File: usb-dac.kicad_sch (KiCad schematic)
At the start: 18 parts, among them P1 USB_C_Plug_USB2.0, U1 PCM2912APJTR, Y1 6 Mhz

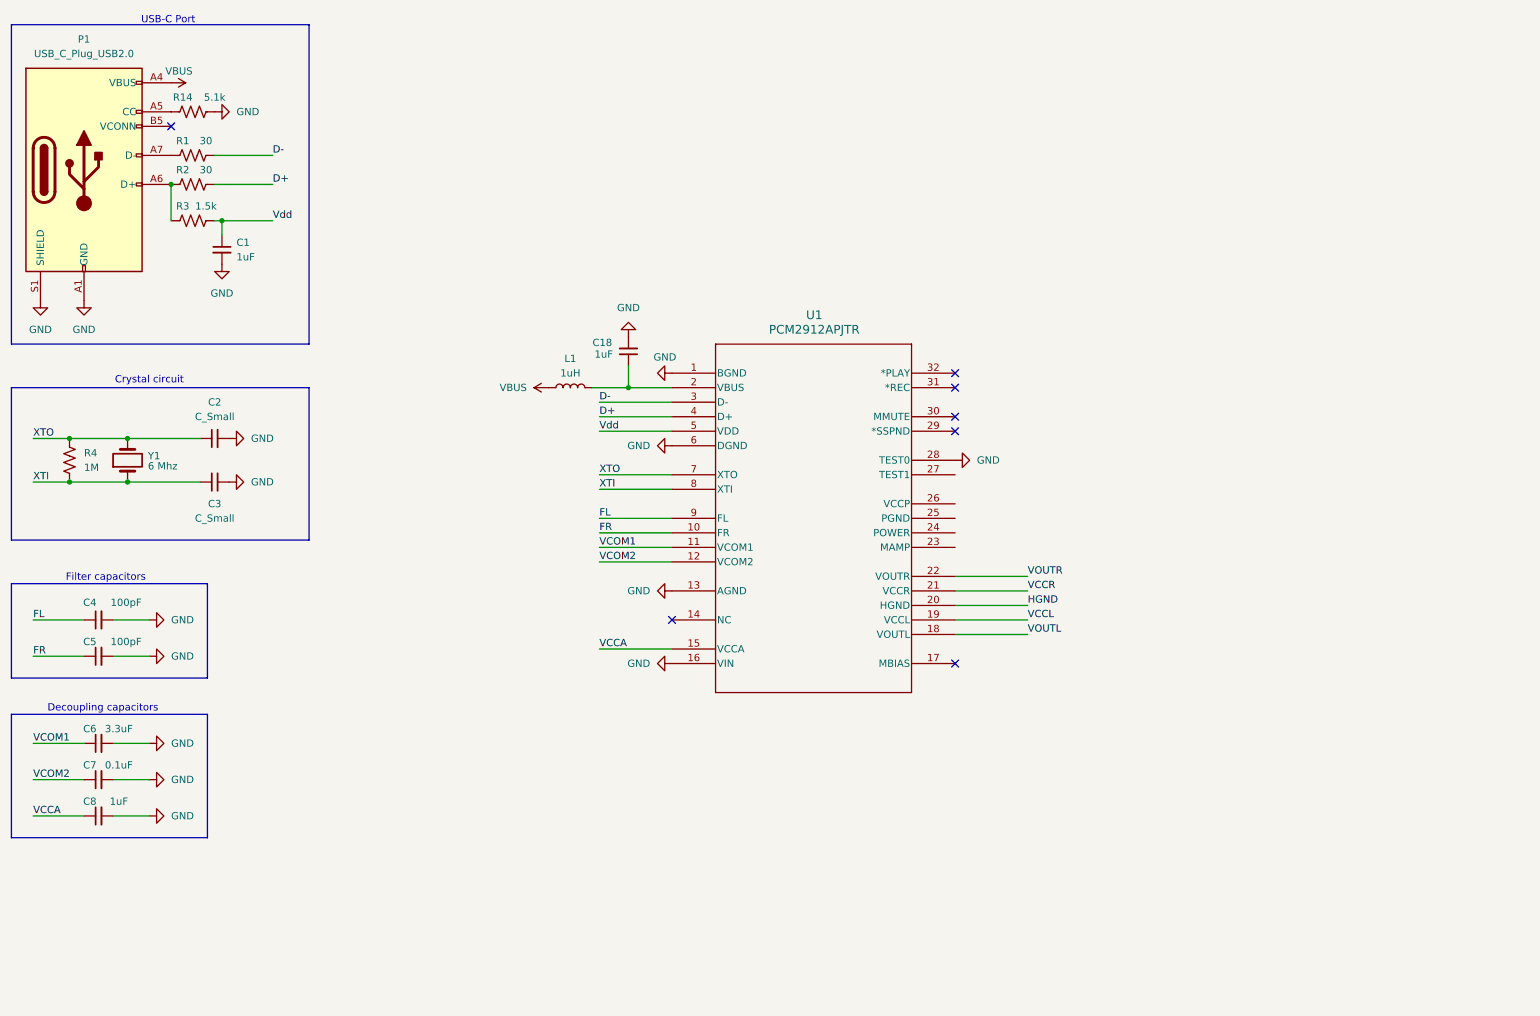
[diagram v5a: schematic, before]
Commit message: More work on schematic Add headphone jack and reduce error amount
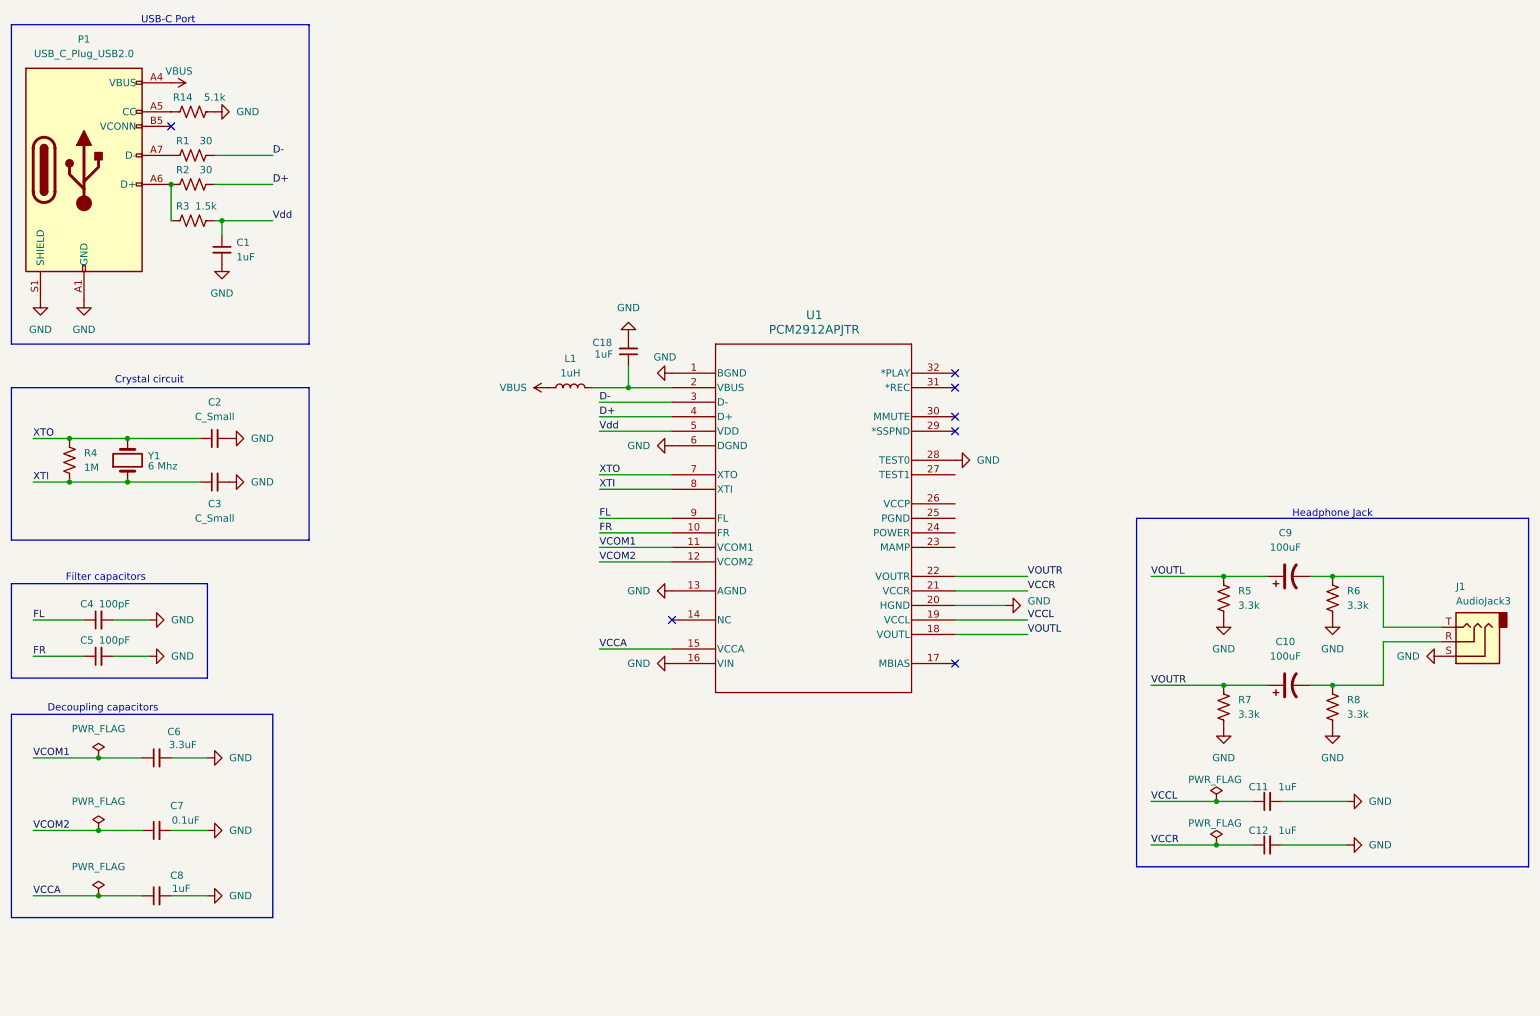
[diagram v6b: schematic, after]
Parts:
- added C10, C9: 100uF, symbol Device:C_Polarized_US
- added C11, C12: 1uF, symbol Device:C_Small
- added J1: AudioJack3, symbol Connector_Audio:AudioJack3
- added R5, R6, R7, R8: 3.3k, symbol Device:R_US
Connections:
- net HGND is gone; now on net GND: U1.20 (HGND)
- net GND: now also C11.2, C12.2, J1.S, R5.2, R6.2, R7.2, R8.2
- net VCCL: now also C11.1
- net VCCR: now also C12.1
- net VOUTL: now also C9.1, R5.1
- net VOUTR: now also C10.1, R7.1
- new net: C10.2, J1.R, R8.1
- new net: C9.2, J1.T, R6.1
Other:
- note added: "Headphone Jack"
- moved on the sheet: C6, C7, C8

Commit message: Finish schematic
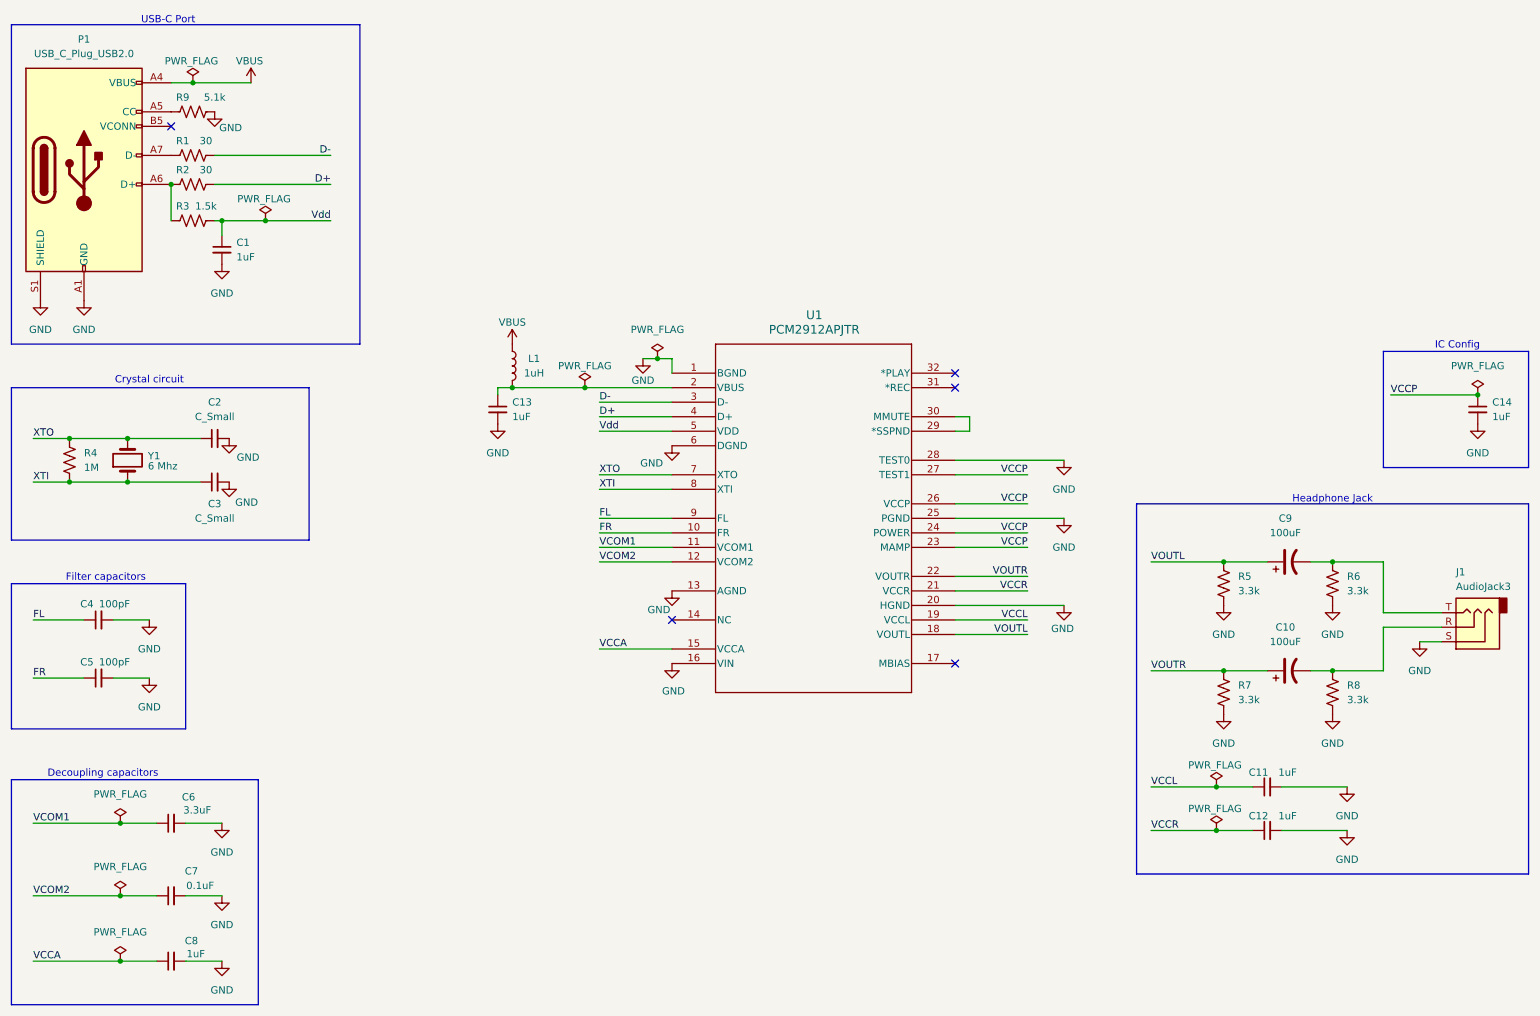
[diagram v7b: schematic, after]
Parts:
- removed C18: 1uF, symbol Device:C_Small
- added C13, C14: 1uF, symbol Device:C_Small
- renumbered R14 to R9
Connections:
- net GND: now also U1.25 (PGND), C13.2, C14.2
- net at L1.2, U1.2 (VBUS): now also C13.1
- net VCCP: now reaches U1.23 (MAMP)
- net VCCP: now also U1.24 (POWER), U1.26 (VCCP), U1.27 (TEST1), C14.1
- net at U1.29 (*SSPND): now also U1.30 (MMUTE)
- no-connect marks 7 -> 5
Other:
- note added: "IC Config"
- moved on the sheet: C10, C11, C12, C5, C6, C7, C8, C9, J1, L1, R5, R6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
